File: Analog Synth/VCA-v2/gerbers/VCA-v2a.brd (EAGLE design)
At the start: 50 x 50 mm, 43 parts, among them IC2 TL084D, T1 DMMT3904W, T2 MMBT2222ALT1

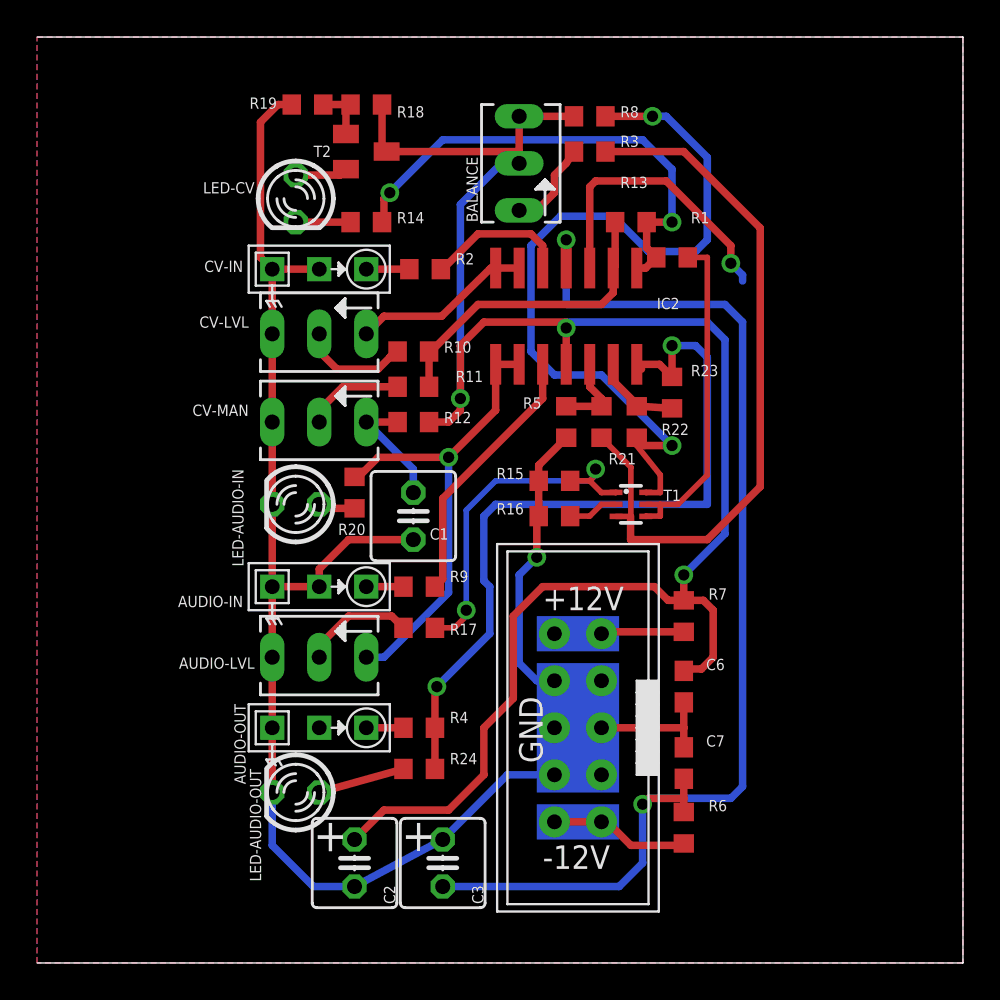
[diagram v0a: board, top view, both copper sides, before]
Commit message: VCA-v2. Using eagle version 7.6 to generate the gerbers because my install of version 6 was having trouble finding its output devices... whatever that means...
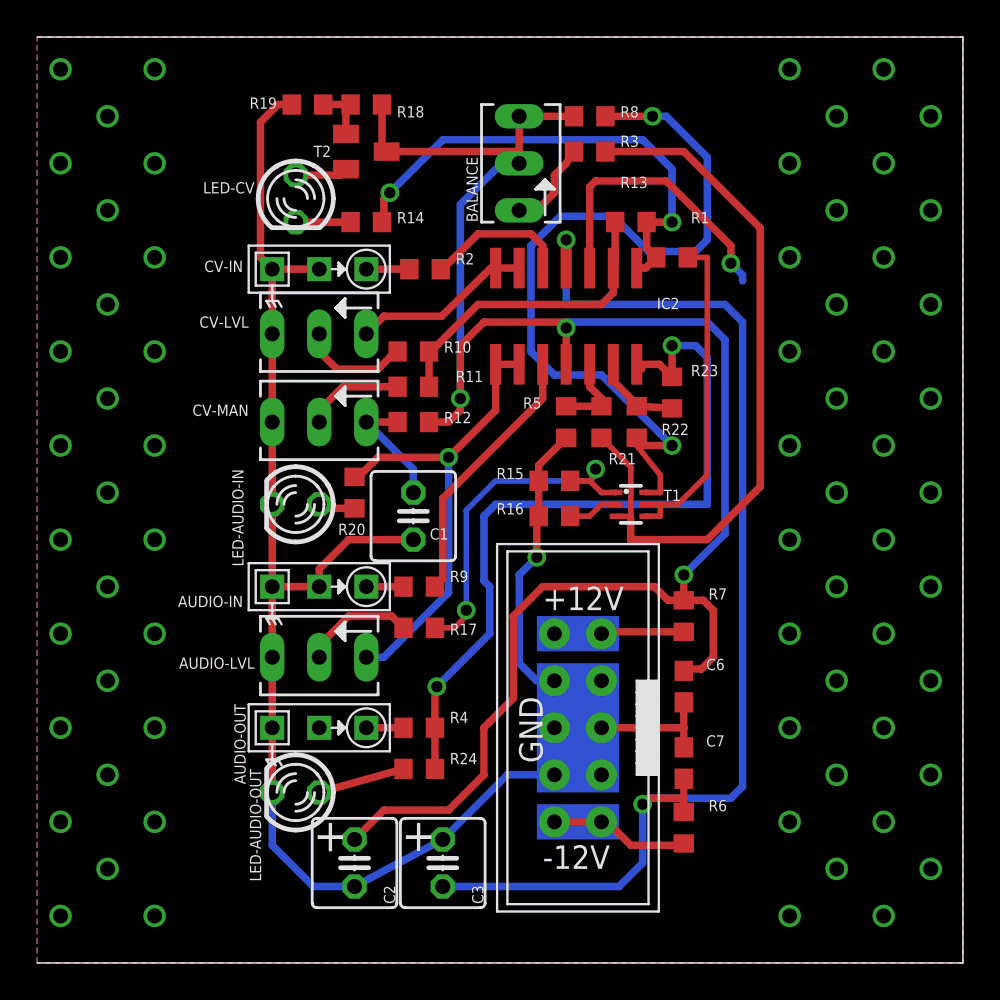
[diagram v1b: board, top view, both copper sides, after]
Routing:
- net GND: vias 2 -> 69
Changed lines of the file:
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@@
 <?xml version="1.0" encoding="utf-8"?>
 <!DOCTYPE eagle SYSTEM "eagle.dtd">
-<eagle version="6.6.0">
+<eagle version="7.6.0">
 <drawing>
 <settings>
@@
 <text x="19.685" y="6.0325" size="1.778" layer="25">+</text>
 <text x="14.9225" y="6.0325" size="1.778" layer="25">+</text>
-<rectangle x1="0" y1="0" x2="7.3025" y2="49.8475" layer="39"/>
-<rectangle x1="40.005" y1="0" x2="49.8475" y2="49.8475" layer="39"/>
-<rectangle x1="0" y1="0" x2="7.3025" y2="49.8475" layer="40"/>
-<rectangle x1="40.005" y1="0" x2="49.8475" y2="49.8475" layer="40"/>
+<rectangle x1="0" y1="0" x2="7.3025" y2="49.8475" layer="29"/>
+<rectangle x1="40.005" y1="0" x2="49.8475" y2="49.8475" layer="29"/>
+<rectangle x1="0" y1="0" x2="7.3025" y2="49.8475" layer="30"/>
+<rectangle x1="40.005" y1="0" x2="49.8475" y2="49.8475" layer="30"/>
 </plain>
 <attributes>
@@
 <pass name="Default">
 <param name="RoutingGrid" value="50mil"/>
+<param name="AutoGrid" value="1"/>
+<param name="Efforts" value="0"/>
+<param name="TopRouterVariant" value="1"/>
 <param name="tpViaShape" value="round"/>
 <param name="PrefDir.1" value="|"/>
@@
 <vertex x="50" y="0"/>
 </polygon>
+<via x="1.27" y="33.02" extent="1-16" drill="0.8128"/>
+<via x="3.81" y="30.48" extent="1-16" drill="0.8128"/>
+<via x="1.27" y="27.94" extent="1-16" drill="0.8128"/>
+<via x="3.81" y="25.4" extent="1-16" drill="0.8128"/>
+<via x="1.27" y="22.86" extent="1-16" drill="0.8128"/>
+<via x="3.81" y="20.32" extent="1-16" drill="0.8128"/>
+<via x="1.27" y="17.78" extent="1-16" drill="0.8128"/>
+<via x="3.81" y="15.24" extent="1-16" drill="0.8128"/>
+<via x="1.27" y="12.7" extent="1-16" drill="0.8128"/>
+<via x="3.81" y="10.16" extent="1-16" drill="0.8128"/>
+<via x="1.27" y="7.62" extent="1-16" drill="0.8128"/>
+<via x="3.81" y="5.08" extent="1-16" drill="0.8128"/>
+<via x="1.27" y="2.54" extent="1-16" drill="0.8128"/>
+<via x="6.35" y="17.78" extent="1-16" drill="0.8128"/>
+<via x="6.35" y="12.7" extent="1-16" drill="0.8128"/>
+<via x="6.35" y="7.62" extent="1-16" drill="0.8128"/>
+<via x="6.35" y="2.54" extent="1-16" drill="0.8128"/>
+<via x="6.35" y="33.02" extent="1-16" drill="0.8128"/>
+<via x="6.35" y="27.94" extent="1-16" drill="0.8128"/>
+<via x="6.35" y="22.86" extent="1-16" drill="0.8128"/>
+<via x="1.27" y="48.26" extent="1-16" drill="0.8128"/>
+<via x="3.81" y="45.72" extent="1-16" drill="0.8128"/>
+<via x="1.27" y="43.18" extent="1-16" drill="0.8128"/>
+<via x="3.81" y="40.64" extent="1-16" drill="0.8128"/>
+<via x="1.27" y="38.1" extent="1-16" drill="0.8128"/>
+<via x="3.81" y="35.56" extent="1-16" drill="0.8128"/>
+<via x="6.35" y="48.26" extent="1-16" drill="0.8128"/>
+<via x="6.35" y="43.18" extent="1-16" drill="0.8128"/>
+<via x="6.35" y="38.1" extent="1-16" drill="0.8128"/>
+<via x="40.64" y="48.26" extent="1-16" drill="0.8128"/>
+<via x="43.18" y="45.72" extent="1-16" drill="0.8128"/>
+<via x="40.64" y="43.18" extent="1-16" drill="0.8128"/>
+<via x="43.18" y="40.64" extent="1-16" drill="0.8128"/>
+<via x="40.64" y="38.1" extent="1-16" drill="0.8128"/>
+<via x="43.18" y="35.56" extent="1-16" drill="0.8128"/>
+<via x="45.72" y="48.26" extent="1-16" drill="0.8128"/>
+<via x="48.26" y="45.72" extent="1-16" drill="0.8128"/>
+<via x="45.72" y="43.18" extent="1-16" drill="0.8128"/>
+<via x="48.26" y="40.64" extent="1-16" drill="0.8128"/>
+<via x="45.72" y="38.1" extent="1-16" drill="0.8128"/>
+<via x="48.26" y="35.56" extent="1-16" drill="0.8128"/>
+<via x="45.72" y="33.02" extent="1-16" drill="0.8128"/>
+<via x="48.26" y="30.48" extent="1-16" drill="0.8128"/>
+<via x="45.72" y="27.94" extent="1-16" drill="0.8128"/>
+<via x="48.26" y="25.4" extent="1-16" drill="0.8128"/>
+<via x="45.72" y="22.86" extent="1-16" drill="0.8128"/>
+<via x="48.26" y="20.32" extent="1-16" drill="0.8128"/>
+<via x="40.64" y="33.02" extent="1-16" drill="0.8128"/>
+<via x="43.18" y="30.48" extent="1-16" drill="0.8128"/>
+<via x="40.64" y="27.94" extent="1-16" drill="0.8128"/>
+<via x="43.18" y="25.4" extent="1-16" drill="0.8128"/>
+<via x="40.64" y="22.86" extent="1-16" drill="0.8128"/>
+<via x="43.18" y="20.32" extent="1-16" drill="0.8128"/>
+<via x="45.72" y="17.78" extent="1-16" drill="0.8128"/>
+<via x="48.26" y="15.24" extent="1-16" drill="0.8128"/>
+<via x="45.72" y="12.7" extent="1-16" drill="0.8128"/>
+<via x="48.26" y="10.16" extent="1-16" drill="0.8128"/>
+<via x="45.72" y="7.62" extent="1-16" drill="0.8128"/>
+<via x="48.26" y="5.08" extent="1-16" drill="0.8128"/>
+<via x="45.72" y="2.54" extent="1-16" drill="0.8128"/>
+<via x="40.64" y="17.78" extent="1-16" drill="0.8128"/>
+<via x="43.18" y="15.24" extent="1-16" drill="0.8128"/>
+<via x="40.64" y="12.7" extent="1-16" drill="0.8128"/>
+<via x="43.18" y="10.16" extent="1-16" drill="0.8128"/>
+<via x="40.64" y="7.62" extent="1-16" drill="0.8128"/>
+<via x="43.18" y="5.08" extent="1-16" drill="0.8128"/>
+<via x="40.64" y="2.54" extent="1-16" drill="0.8128"/>
+<wire x1="43.18" y1="15.24" x2="40.64" y2="17.78" width="0" layer="19" extent="1-1"/>
+<wire x1="40.64" y1="12.7" x2="43.18" y2="15.24" width="0" layer="19" extent="1-1"/>
+<wire x1="43.18" y1="10.16" x2="40.64" y2="12.7" width="0" layer="19" extent="1-1"/>
+<wire x1="40.64" y1="7.62" x2="43.18" y2="10.16" width="0" layer="19" extent="1-1"/>
+<wire x1="43.18" y1="5.08" x2="40.64" y2="7.62" width="0" layer="19" extent="1-1"/>
+<wire x1="40.64" y1="2.54" x2="43.18" y2="5.08" width="0" layer="19" extent="1-1"/>
+<wire x1="43.18" y1="20.32" x2="40.64" y2="17.78" width="0" layer="19" extent="1-1"/>
 </signal>
 <signal name="+12V">
